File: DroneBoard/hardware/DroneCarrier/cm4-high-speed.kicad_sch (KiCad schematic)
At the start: 5 parts, among them J1 Conn_01x22_Female, J6 THD-02-R

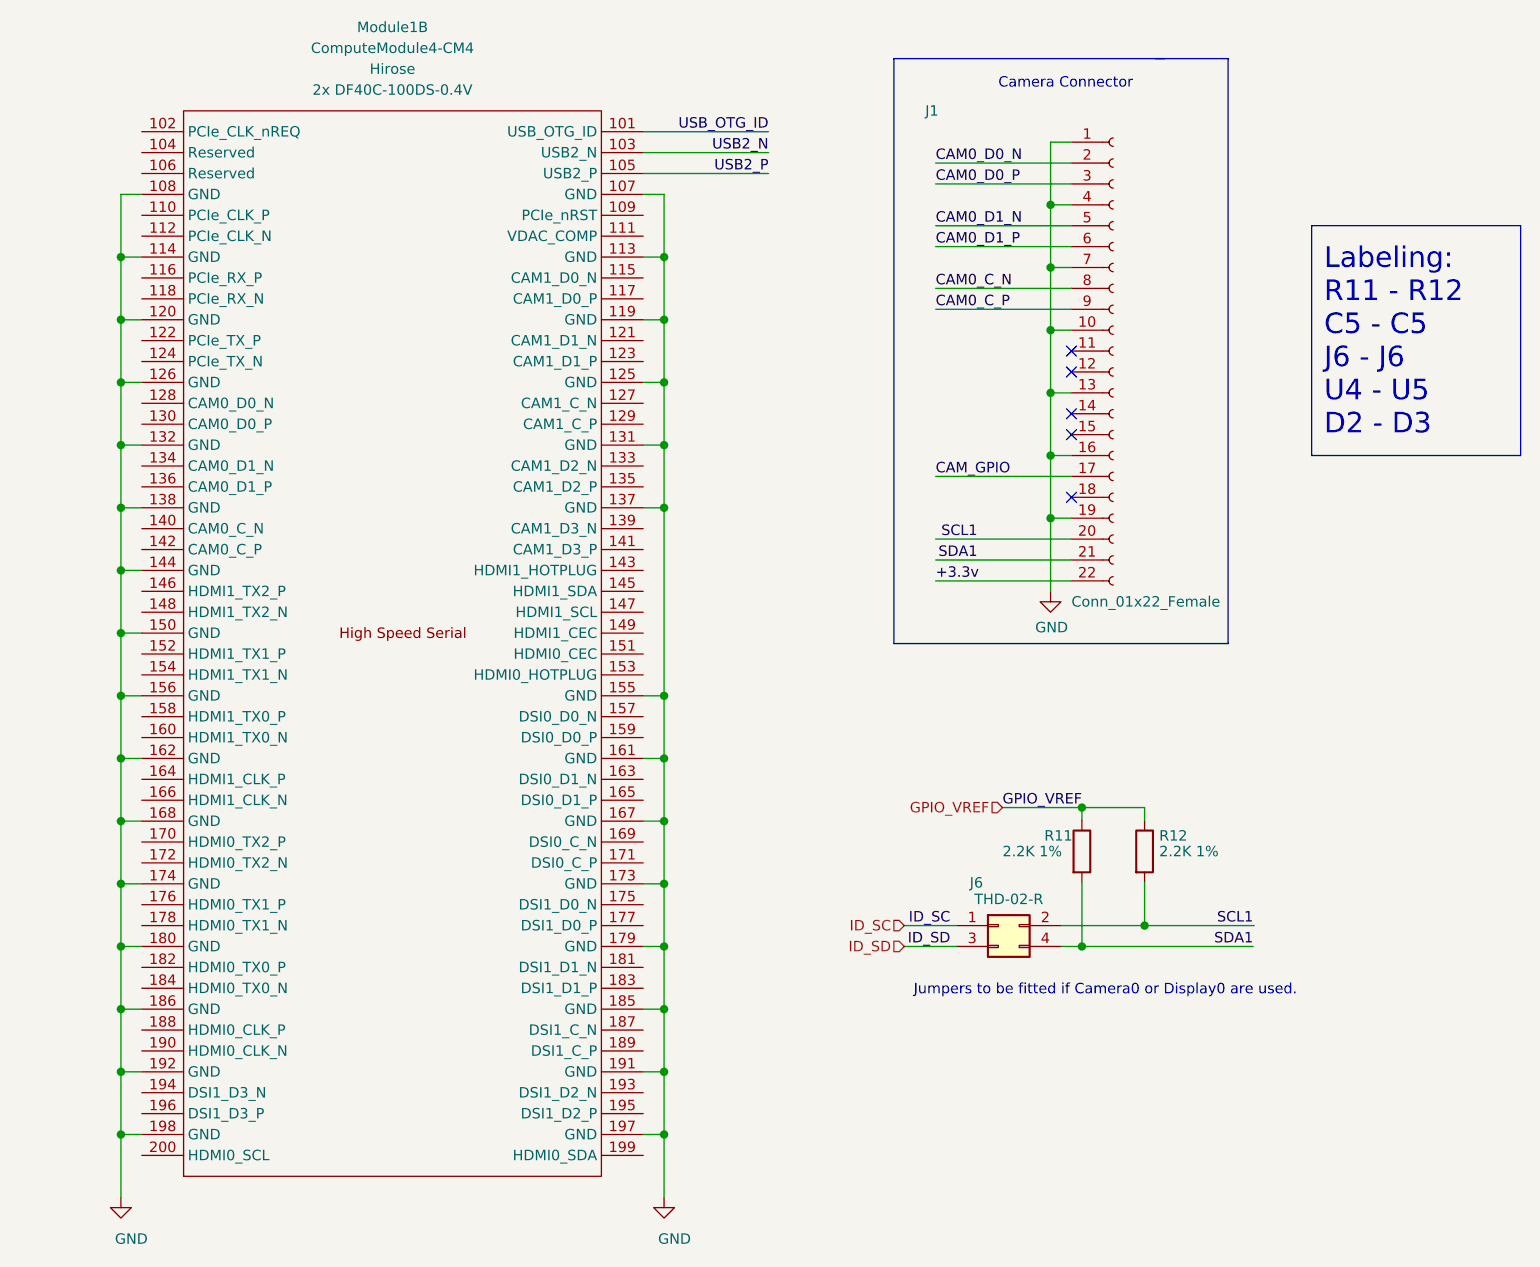
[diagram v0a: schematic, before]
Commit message: Labelling needs to be compared to the RPi CM4
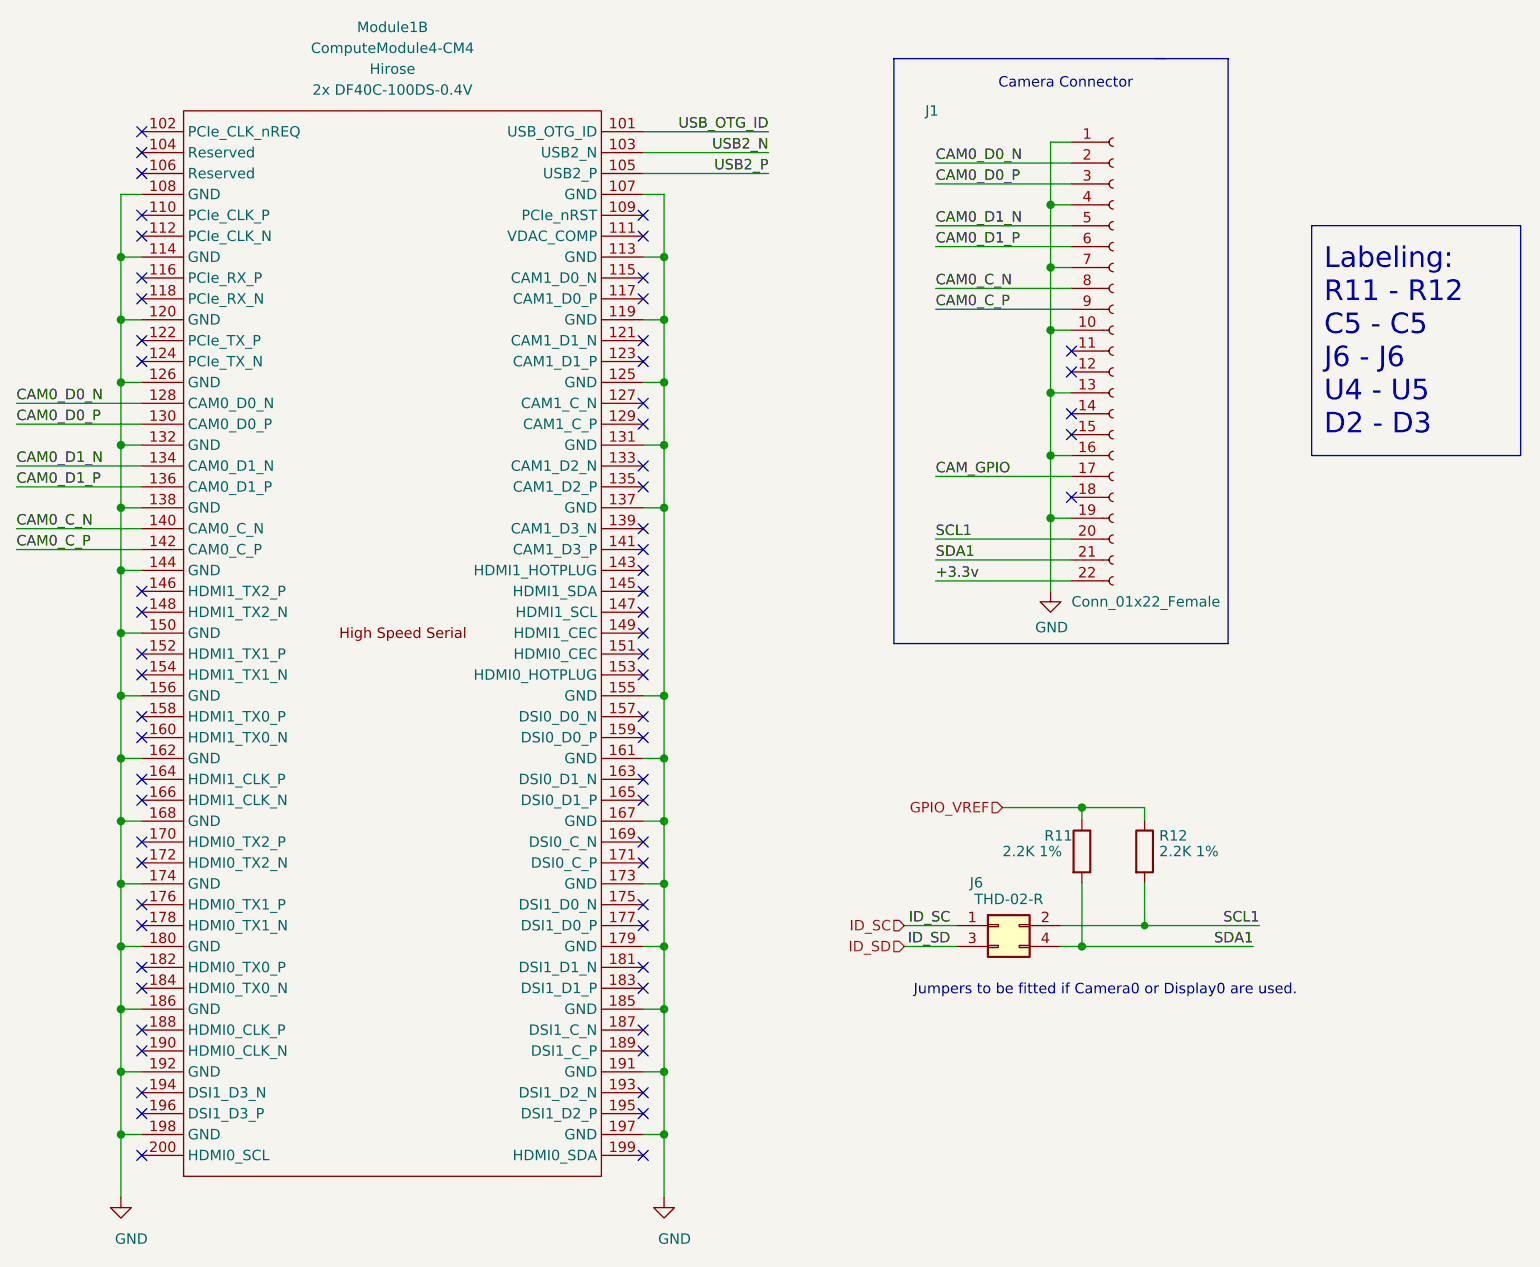
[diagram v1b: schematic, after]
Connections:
- net CAM0_C_N: now also Module1.140 (CAM0_C_N)
- net CAM0_C_P: now also Module1.142 (CAM0_C_P)
- net CAM0_D0_N: now also Module1.128 (CAM0_D0_N)
- net CAM0_D0_P: now also Module1.130 (CAM0_D0_P)
- net CAM0_D1_N: now also Module1.134 (CAM0_D1_N)
- net CAM0_D1_P: now also Module1.136 (CAM0_D1_P)
- no-connect marks 5 -> 66
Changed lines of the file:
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@@
   (junction (at 157.48 127.889) (diameter 1.016) (color 0 0 0 0))
   (junction (at 157.48 144.78) (diameter 1.016) (color 0 0 0 0))
-  (junction (at 165.1 142.24) (diameter 1.016) (color 0 0 0 0))
+  (junction (at 165.1 142.24) (diameter 0) (color 0 0 0 0))
+  (no_connect (at 43.18 45.72))
+  (no_connect (at 43.18 48.26))
+  (no_connect (at 43.18 50.8))
+  (no_connect (at 43.18 55.88))
+  (no_connect (at 43.18 58.42))
+  (no_connect (at 43.18 63.5))
+  (no_connect (at 43.18 66.04))
+  (no_connect (at 43.18 71.12))
+  (no_connect (at 43.18 73.66))
+  (no_connect (at 43.18 101.6))
+  (no_connect (at 43.18 104.14))
+  (no_connect (at 43.18 109.22))
+  (no_connect (at 43.18 111.76))
+  (no_connect (at 43.18 116.84))
+  (no_connect (at 43.18 119.38))
+  (no_connect (at 43.18 124.46))
+  (no_connect (at 43.18 127))
+  (no_connect (at 43.18 132.08))
+  (no_connect (at 43.18 134.62))
+  (no_connect (at 43.18 139.7))
+  (no_connect (at 43.18 142.24))
+  (no_connect (at 43.18 147.32))
+  (no_connect (at 43.18 149.86))
+  (no_connect (at 43.18 154.94))
+  (no_connect (at 43.18 157.48))
+  (no_connect (at 43.18 162.56))
+  (no_connect (at 43.18 165.1))
+  (no_connect (at 43.18 170.18))
+  (no_connect (at 104.14 55.88))
+  (no_connect (at 104.14 58.42))
+  (no_connect (at 104.14 63.5))
+  (no_connect (at 104.14 66.04))
+  (no_connect (at 104.14 71.12))
+  (no_connect (at 104.14 73.66))
+  (no_connect (at 104.14 78.74))
+  (no_connect (at 104.14 81.28))
+  (no_connect (at 104.14 86.36))
+  (no_connect (at 104.14 88.9))
+  (no_connect (at 104.14 93.98))
+  (no_connect (at 104.14 96.52))
+  (no_connect (at 104.14 99.06))
+  (no_connect (at 104.14 101.6))
+  (no_connect (at 104.14 104.14))
+  (no_connect (at 104.14 106.68))
+  (no_connect (at 104.14 109.22))
+  (no_connect (at 104.14 111.76))
+  (no_connect (at 104.14 116.84))
+  (no_connect (at 104.14 119.38))
+  (no_connect (at 104.14 124.46))
+  (no_connect (at 104.14 127))
+  (no_connect (at 104.14 132.08))
+  (no_connect (at 104.14 134.62))
+  (no_connect (at 104.14 139.7))
+  (no_connect (at 104.14 142.24))
+  (no_connect (at 104.14 147.32))
+  (no_connect (at 104.14 149.86))
+  (no_connect (at 104.14 154.94))
+  (no_connect (at 104.14 157.48))
+  (no_connect (at 104.14 162.56))
+  (no_connect (at 104.14 165.1))
+  (no_connect (at 104.14 170.18))
   (no_connect (at 156.21 72.39))
   (no_connect (at 156.21 74.93))
@@
   (no_connect (at 156.21 82.55))
   (no_connect (at 156.21 90.17))
+  (wire (pts (xy 27.94 78.74) (xy 43.18 78.74))
+    (stroke (width 0) (type default) (color 0 0 0 0))
+  )
+  (wire (pts (xy 27.94 81.28) (xy 43.18 81.28))
+    (stroke (width 0) (type default) (color 0 0 0 0))
+  )
+  (wire (pts (xy 27.94 86.36) (xy 43.18 86.36))
+    (stroke (width 0) (type default) (color 0 0 0 0))
+  )
+  (wire (pts (xy 27.94 88.9) (xy 43.18 88.9))
+    (stroke (width 0) (type default) (color 0 0 0 0))
+  )
+  (wire (pts (xy 27.94 93.98) (xy 43.18 93.98))
+    (stroke (width 0) (type default) (color 0 0 0 0))
+  )
+  (wire (pts (xy 27.94 96.52) (xy 43.18 96.52))
+    (stroke (width 0) (type default) (color 0 0 0 0))
+  )
   (wire (pts (xy 40.64 53.34) (xy 40.64 60.96))
     (stroke (width 0) (type solid) (color 0 0 0 0))
@@
     (stroke (width 0) (type solid) (color 0 0 0 0))
   )
-  (wire (pts (xy 165.1 142.24) (xy 178.435 142.24))
-    (stroke (width 0) (type solid) (color 0 0 0 0))
+  (wire (pts (xy 165.1 142.24) (xy 179.07 142.24))
+    (stroke (width 0) (type default) (color 0 0 0 0))
   )
   (polyline (pts (xy 134.62 36.83) (xy 134.62 107.95))
@@
     (effects (font (size 2.5 2.5)) (justify left bottom))
   )
+  (label "CAM0_D0_N" (at 27.94 78.74 0)
+    (effects (font (size 1.27 1.27)) (justify left bottom))
+  )
+  (label "CAM0_D0_P" (at 27.94 81.28 0)
+    (effects (font (size 1.27 1.27)) (justify left bottom))
+  )
+  (label "CAM0_D1_N" (at 27.94 86.36 0)
+    (effects (font (size 1.27 1.27)) (justify left bottom))
+  )
+  (label "CAM0_D1_P" (at 27.94 88.9 0)
+    (effects (font (size 1.27 1.27)) (justify left bottom))
+  )
+  (label "CAM0_C_N" (at 27.94 93.98 0)
+    (effects (font (size 1.27 1.27)) (justify left bottom))
+  )
+  (label "CAM0_C_P" (at 27.94 96.52 0)
+    (effects (font (size 1.27 1.27)) (justify left bottom))
+  )
   (label "USB_OTG_ID" (at 119.38 45.72 180)
     (effects (font (size 1.27 1.27)) (justify right bottom))
@@
     (effects (font (size 1.27 1.27)) (justify left bottom))
   )
+  (label "SCL1" (at 139.7 95.25 0)
+    (effects (font (size 1.27 1.27)) (justify left bottom))
+  )
+  (label "SDA1" (at 139.7 97.79 0)
+    (effects (font (size 1.27 1.27)) (justify left bottom))
+  )
   (label "+3.3v" (at 139.7 100.33 0)
     (effects (font (size 1.27 1.27)) (justify left bottom))
@@
     (effects (font (size 1.27 1.27)) (justify right bottom))
   )
-  (label "SCL1" (at 144.78 95.25 180)
-    (effects (font (size 1.27 1.27)) (justify right bottom))
-  )
-  (label "SDA1" (at 144.78 97.79 180)
-    (effects (font (size 1.27 1.27)) (justify right bottom))
-  )
-  (label "GPIO_VREF" (at 147.828 127.889 0)
-    (effects (font (size 1.27 1.27)) (justify left bottom))
-  )
-  (label "SCL1" (at 178.308 142.24 180)
-    (effects (font (size 1.27 1.27)) (justify right bottom))
-  )
   (label "SDA1" (at 178.308 144.78 180)
+    (effects (font (size 1.27 1.27)) (justify right bottom))
+  )
+  (label "SCL1" (at 179.07 142.24 180)
     (effects (font (size 1.27 1.27)) (justify right bottom))
   )
@@
   (symbol (lib_id "power:GND") (at 153.67 101.6 0) (unit 1)
     (in_bom yes) (on_board yes)
-    (property "Reference" "#PWR?" (id 0) (at 153.67 107.95 0)
-      (effects (font (size 1.27 1.27)) hide)
-    )
+    (property "Reference" "#PWR0121" (id 0) (at 153.67 107.95 0)
+      (effects (font (size 1.27 1.27)) hide)
+    )
